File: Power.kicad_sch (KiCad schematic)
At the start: 24 parts, among them J10 Servo PW 7, J11 Servo PW 8, J3 1986660-2, J4 Servo PW 1, J5 Servo PW 2, J6 Servo PW 3, J7 Servo PW 4, J8 Servo PW 5, J9 Servo PW 6, U4 AP62301WU

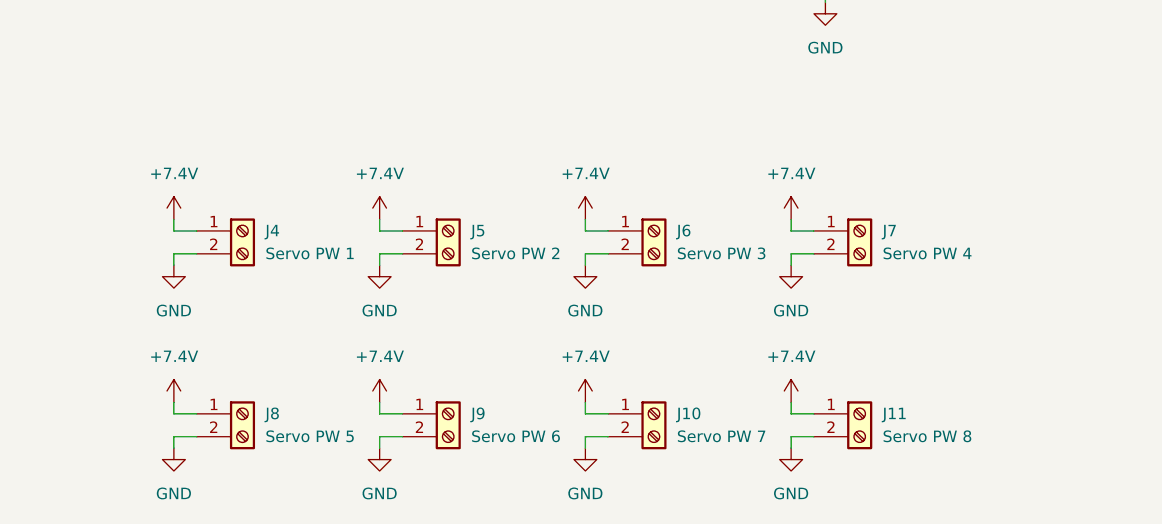
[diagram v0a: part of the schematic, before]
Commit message: Combine servo outputs to 3 pin terminal
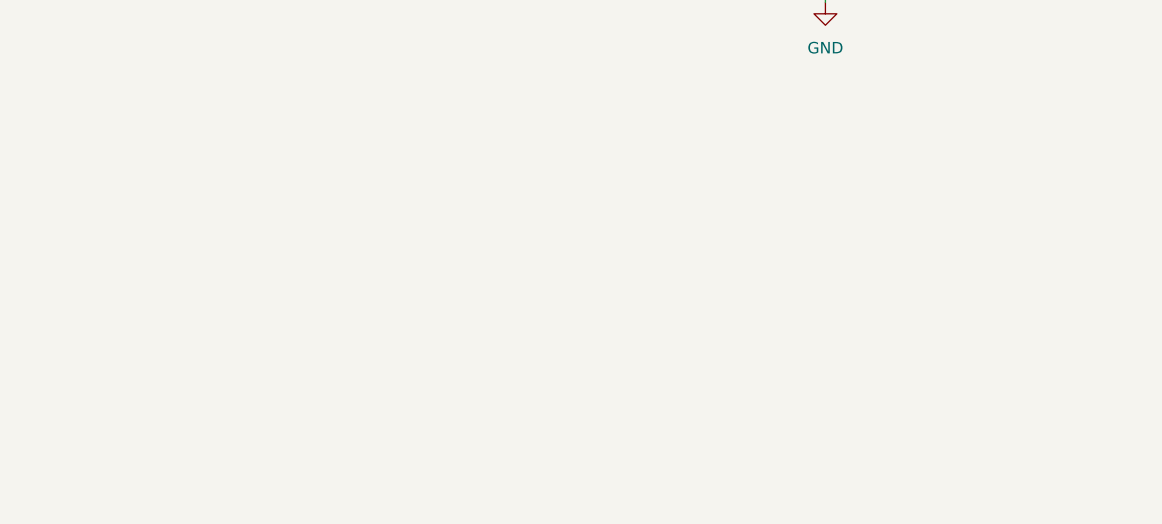
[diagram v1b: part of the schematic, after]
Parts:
- removed J10: Servo PW 7, TerminalBlock_Phoenix:TerminalBlock_Phoenix_MKDS-1,5-2_1x02_P5.00mm_Horizontal, symbol Connector:Screw_Terminal_01x02
- removed J11: Servo PW 8, TerminalBlock_Phoenix:TerminalBlock_Phoenix_MKDS-1,5-2_1x02_P5.00mm_Horizontal, symbol Connector:Screw_Terminal_01x02
- removed J4: Servo PW 1, TerminalBlock_Phoenix:TerminalBlock_Phoenix_MKDS-1,5-2_1x02_P5.00mm_Horizontal, symbol Connector:Screw_Terminal_01x02
- removed J5: Servo PW 2, TerminalBlock_Phoenix:TerminalBlock_Phoenix_MKDS-1,5-2_1x02_P5.00mm_Horizontal, symbol Connector:Screw_Terminal_01x02
- removed J6: Servo PW 3, TerminalBlock_Phoenix:TerminalBlock_Phoenix_MKDS-1,5-2_1x02_P5.00mm_Horizontal, symbol Connector:Screw_Terminal_01x02
- removed J7: Servo PW 4, TerminalBlock_Phoenix:TerminalBlock_Phoenix_MKDS-1,5-2_1x02_P5.00mm_Horizontal, symbol Connector:Screw_Terminal_01x02
- removed J8: Servo PW 5, TerminalBlock_Phoenix:TerminalBlock_Phoenix_MKDS-1,5-2_1x02_P5.00mm_Horizontal, symbol Connector:Screw_Terminal_01x02
- removed J9: Servo PW 6, TerminalBlock_Phoenix:TerminalBlock_Phoenix_MKDS-1,5-2_1x02_P5.00mm_Horizontal, symbol Connector:Screw_Terminal_01x02

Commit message: Add footprints to symbols
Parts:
- C18: footprint (none) -> Capacitor_SMD:C_1210_3225Metric; Listing (none) -> https://www.digikey.com/en/products/detail/samsung-electro-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
- C19, C21: footprint (none) -> Capacitor_SMD:C_1206_3216Metric; Listing (none) -> https://www.digikey.com/en/products/detail/samsung-electro-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
- C20, C24, C25: footprint (none) -> Capacitor_SMD:C_0603_1608Metric; Listing (none) -> https://www.digikey.com/en/products/detail/samsung-electro-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
- C22: footprint (none) -> Capacitor_SMD:C_0402_1005Metric; Listing (none) -> https://www.digikey.com/en/products/detail/samsung-electro-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
- C23: footprint (none) -> Capacitor_SMD:C_0402_1005Metric; Listing (none) -> https://www.digikey.com/en/products/detail/murata-electroni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
- CR1, U4: Listing (none) -> https://www.digikey.com/en/products/detail/diodes-incorpora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
- CR2: Listing (none) -> https://www.digikey.com/en/products/detail/vishay-general-s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
- D2: Listing (none) -> https://www.digikey.com/en/products/detail/microchip-techno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
- J3: Listing (none) -> https://www.digikey.com/en/products/detail/te-connectivity-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
- L1: footprint (none) -> Inductor_SMD:L_0805_2012Metric; Listing (none) -> https://www.digikey.com/en/products/detail/tdk-corporation/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
- R10: footprint (none) -> Resistor_SMD:R_0402_1005Metric; Listing (none) -> https://www.digikey.com/en/products/detail/stackpole-electr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
- R11: footprint (none) -> Resistor_SMD:R_0402_1005Metric; Listing (none) -> https://www.digikey.com/en/products/detail/yageo/RC0402FR-0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
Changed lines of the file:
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@@
 			)
 		)
-		(property "Footprint" ""
+		(property "Footprint" "Capacitor_SMD:C_0603_1608Metric"
 			(at 110.1852 48.26 0)
 			(effects
@@
 			)
 		)
-		(property "Datasheet" "~"
+		(property "Datasheet" "https://weblib.samsungsem.com/mlcc/mlcc-ec-data-sheet.do?partNumber=CL10B105KO8NNN"
 			(at 109.22 44.45 0)
 			(effects
@@
 		)
 		(property "Description" "Unpolarized capacitor"
+			(at 109.22 44.45 0)
+			(effects
+				(font
+					(size 1.27 1.27)
+				)
+				(hide yes)
+			)
+		)
+		(property "Listing" "https://www.digikey.com/en/products/detail/samsung-electro-mechanics/CL10B105KO8NNNC/3886677"
 			(at 109.22 44.45 0)
 			(effects
@@
 			)
 		)
-		(property "Footprint" ""
+		(property "Footprint" "Capacitor_SMD:C_0402_1005Metric"
 			(at 87.3252 102.87 0)
 			(effects
@@
 			)
 		)
-		(property "Datasheet" "~"
+		(property "Datasheet" "https://search.murata.co.jp/Ceramy/image/img/A01X/G101/ENG/GJM1555C1H100GB01-01.pdf"
 			(at 86.36 99.06 0)
 			(effects
@@
 		)
 		(property "Description" "Unpolarized capacitor"
+			(at 86.36 99.06 0)
+			(effects
+				(font
+					(size 1.27 1.27)
+				)
+				(hide yes)
+			)
+		)
+		(property "Listing" "https://www.digikey.com/en/products/detail/murata-electronics/GJM1555C1H100GB01D/2592846"
 			(at 86.36 99.06 0)
 			(effects
@@
 			)
 		)
+		(property "Listing" "https://www.digikey.com/en/products/detail/microchip-technology/APT60S20BG/1494822"
+			(at 67.31 40.64 0)
+			(effects
+				(font
+					(size 1.27 1.27)
+				)
+				(hide yes)
+			)
+		)
 		(pin "1"
 		)
@@
 			)
 		)
-		(property "Footprint" ""
+		(property "Footprint" "Capacitor_SMD:C_0603_1608Metric"
 			(at 115.2652 107.95 0)
 			(effects
@@
 			)
 		)
-		(property "Datasheet" "~"
+		(property "Datasheet" "https://mm.digikey.com/Volume0/opasdata/d220001/medias/docus/2901/CL10A226MP8NUNC_Spec.pdf"
 			(at 114.3 104.14 0)
 			(effects
@@
 		)
 		(property "Description" "Unpolarized capacitor"
+			(at 114.3 104.14 0)
+			(effects
+				(font
+					(size 1.27 1.27)
+				)
+				(hide yes)
+			)
+		)
+		(property "Listing" "https://www.digikey.com/en/products/detail/samsung-electro-mechanics/CL10A226MP8NUNE/3886932"
 			(at 114.3 104.14 0)
 			(effects
@@
 			)
 		)
-		(property "Footprint" ""
+		(property "Footprint" "Capacitor_SMD:C_1210_3225Metric"
 			(at 84.7852 48.26 0)
 			(effects
@@
 			)
 		)
-		(property "Datasheet" "~"
+		(property "Datasheet" "https://mm.digikey.com/Volume0/opasdata/d220001/medias/docus/42/CL32A107MPVNNNE_Spec.pdf"
 			(at 83.82 44.45 0)
 			(effects
@@
 		)
 		(property "Description" "Unpolarized capacitor"
+			(at 83.82 44.45 0)
+			(effects
+				(font
+					(size 1.27 1.27)
+				)
+				(hide yes)
+			)
+		)
+		(property "Listing" "https://www.digikey.com/en/products/detail/samsung-electro-mechanics/CL32A107MPVNNNE/3889022"
 			(at 83.82 44.45 0)
 			(effects
@@
 			)
 		)
-		(property "Footprint" ""
+		(property "Footprint" "Capacitor_SMD:C_1206_3216Metric"
 			(at 37.1348 102.87 0)
 			(effects
@@
 			)
 		)
-		(property "Datasheet" "~"
+		(property "Datasheet" "https://mm.digikey.com/Volume0/opasdata/d220001/medias/docus/658/CL31B106KAHNNNE_Spec.pdf"
 			(at 38.1 99.06 0)
 			(effects
@@
 		)
 		(property "Description" "Unpolarized capacitor"
+			(at 38.1 99.06 0)
+			(effects
+				(font
+					(size 1.27 1.27)
+				)
+				(hide yes)
+			)
+		)
+		(property "Listing" "https://www.digikey.com/en/products/detail/samsung-electro-mechanics/CL31B106KAHNNNE/3887462"
 			(at 38.1 99.06 0)
 			(effects
@@
 			)
 		)
-		(property "Footprint" ""
+		(property "Footprint" "Inductor_SMD:L_0805_2012Metric"
 			(at 80.01 93.98 0)
 			(effects
@@
 			)
 		)
-		(property "Datasheet" "~"
+		(property "Datasheet" "https://product.tdk.com/en/system/files/dam/doc/product/inductor/inductor/smd/catalog/inductor_automotive_decoupling_mlz2012-a_en.pdf"
 			(at 80.01 93.98 0)
 			(effects
@@
 		(property "Description" "Inductor"
 			(at 80.01 93.98 0)
+			(effects
+				(font
+					(size 1.27 1.27)
+				)
+				(hide yes)
+			)
+		)
+		(property "Listing" "https://www.digikey.com/en/products/detail/tdk-corporation/MLZ2012M3R3ATD69/9605952"
+			(at 80.01 93.98 90)
 			(effects
 				(font
@@
 			)
 		)
-		(property "Footprint" ""
+		(property "Footprint" "Resistor_SMD:R_0402_1005Metric"
 			(at 103.886 109.474 90)
 			(effects
@@
 			)
 		)
-		(property "Datasheet" "~"
+		(property "Datasheet" "https://www.yageogroup.com/content/datasheet/asset/file/PYU-RC_GROUP_51_ROHS_L"
 			(at 102.87 109.22 0)
 			(effects
@@
 		)
 		(property "Description" "Resistor, US symbol"
+			(at 102.87 109.22 0)
+			(effects
+				(font
+					(size 1.27 1.27)
+				)
+				(hide yes)
+			)
+		)
+		(property "Listing" "https://www.digikey.com/en/products/detail/yageo/RC0402FR-0710KL/726523"
 			(at 102.87 109.22 0)
 			(effects
@@
 			)
 		)
+		(property "Listing" "https://www.digikey.com/en/products/detail/diodes-incorporated/AP62301WU-7/12349279?s=N4IgTCBcDaIIIAUBsYDMAGAjAdQKogF0BfIA"
+			(at 55.88 96.52 0)
+			(effects
+				(font
+					(size 1.27 1.27)
+				)
+				(hide yes)
+			)
+		)
 		(pin "3"
 		)
@@
 			)
 		)
-		(property "Footprint" ""
+		(property "Footprint" "Capacitor_SMD:C_0603_1608Metric"
 			(at 127.9652 107.95 0)
 			(effects
@@
 			)
 		)
-		(property "Datasheet" "~"
+		(property "Datasheet" "https://mm.digikey.com/Volume0/opasdata/d220001/medias/docus/2901/CL10A226MP8NUNC_Spec.pdf"
 			(at 127 104.14 0)
 			(effects
@@
 		)
 		(property "Description" "Unpolarized capacitor"
+			(at 127 104.14 0)
+			(effects
+				(font
+					(size 1.27 1.27)
+				)
+				(hide yes)
+			)
+		)
+		(property "Listing" "https://www.digikey.com/en/products/detail/samsung-electro-mechanics/CL10A226MP8NUNE/3886932"
 			(at 127 104.14 0)
 			(effects
@@
 			)
 		)
-		(property "Footprint" ""
+		(property "Footprint" "Resistor_SMD:R_0402_1005Metric"
 			(at 103.886 99.314 90)
 			(effects
@@
 			)
 		)
-		(property "Datasheet" "~"
+		(property "Datasheet" "https://www.seielect.com/catalog/SEI-RMCF_RMCP.pdf"
 			(at 102.87 99.06 0)
 			(effects
@@
 		)
 		(property "Description" "Resistor, US symbol"
+			(at 102.87 99.06 0)
+			(effects
+				(font
+					(size 1.27 1.27)
+				)
+				(hide yes)
+			)
+		)
+		(property "Listing" "https://www.digikey.com/en/products/detail/stackpole-electronics-inc/RMCF0402FT31K6/1714647"
 			(at 102.87 99.06 0)
 			(effects
@@
 			)
 		)
+		(property "Listing" "https://www.digikey.com/en/products/detail/vishay-general-semiconductor-diodes-division/MSP3V3-M3-89A/2071748"
+			(at 143.51 104.14 90)
+			(effects
+				(font
+					(size 1.27 1.27)
+				)
+				(hide yes)
+			)
+		)
 		(pin "2"
 		)
@@
 			)
 		)
-		(property "Footprint" ""
+		(property "Footprint" "Capacitor_SMD:C_0402_1005Metric"
 			(at 74.93 87.9348 0)
 			(effects
@@
 			)
 		)
-		(property "Datasheet" "~"
+		(property "Datasheet" "https://mm.digikey.com/Volume0/opasdata/d220001/medias/docus/503/CL05A104KA5NNNC.pdf"
 			(at 71.12 88.9 0)
 			(effects
@@
 		(property "Description" "Unpolarized capacitor"
 			(at 71.12 88.9 0)
+			(effects
+				(font
+					(size 1.27 1.27)
+				)
+				(hide yes)
+			)
+		)
+		(property "Listing" "https://www.digikey.com/en/products/detail/samsung-electro-mechanics/CL05A104KA5NNNC/3886701"
+			(at 71.12 88.9 90)
 			(effects
 				(font
@@
 			)
 		)
-		(property "Footprint" ""
+		(property "Footprint" "Capacitor_SMD:C_1206_3216Metric"
 			(at 97.4852 48.26 0)
 			(effects
@@
 			)
 		)
-		(property "Datasheet" "~"
+		(property "Datasheet" "https://mm.digikey.com/Volume0/opasdata/d220001/medias/docus/658/CL31B106KAHNNNE_Spec.pdf"
 			(at 96.52 44.45 0)
 			(effects
@@
 		)
 		(property "Description" "Unpolarized capacitor"
+			(at 96.52 44.45 0)
+			(effects
+				(font
+					(size 1.27 1.27)
+				)
+				(hide yes)
+			)
+		)
+		(property "Listing" "https://www.digikey.com/en/products/detail/samsung-electro-mechanics/CL31B106KAHNNNE/3887462"
 			(at 96.52 44.45 0)
 			(effects
@@
 			)
 		)
+		(property "Listing" "https://www.digikey.com/en/products/detail/te-connectivity-amp-connectors/1986660-2/4021603"
+			(at 44.45 44.45 0)
+			(effects
+				(font
+					(size 1.27 1.27)
+				)
+				(hide yes)
+			)
+		)
 		(pin "2B"
 		)
@@
 			(effects
 				(font
+					(size 1.27 1.27)
+				)
+				(hide yes)
+			)
+		)
+		(property "Listing" "https://www.digikey.com/en/products/detail/diodes-incorporated/SMBJ7-5A-13-F/749992"
+			(at 76.2 53.34 90)
+			(effects
+				(font

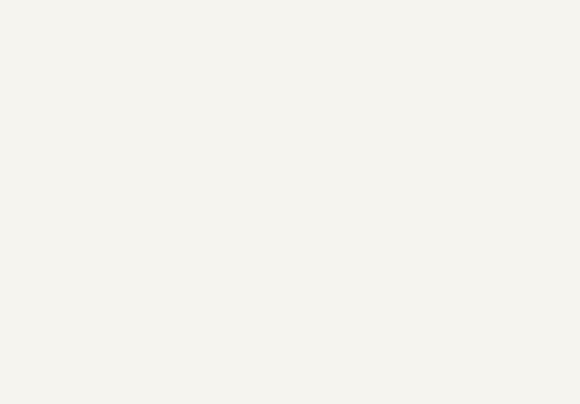
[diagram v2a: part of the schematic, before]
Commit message: Add test points
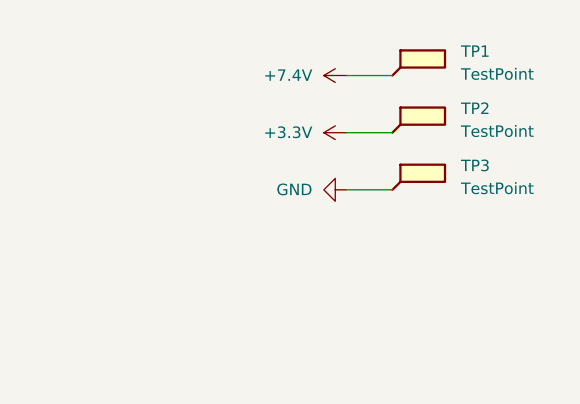
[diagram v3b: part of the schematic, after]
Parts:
- added TP1, TP2, TP3: TestPoint, TestPoint:TestPoint_Plated_Hole_D2.0mm, symbol Connector:TestPoint_Flag
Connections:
- net +3.3V: now also TP2.1
- net +7.4V: now also TP1.1
- net GND: now also TP3.1

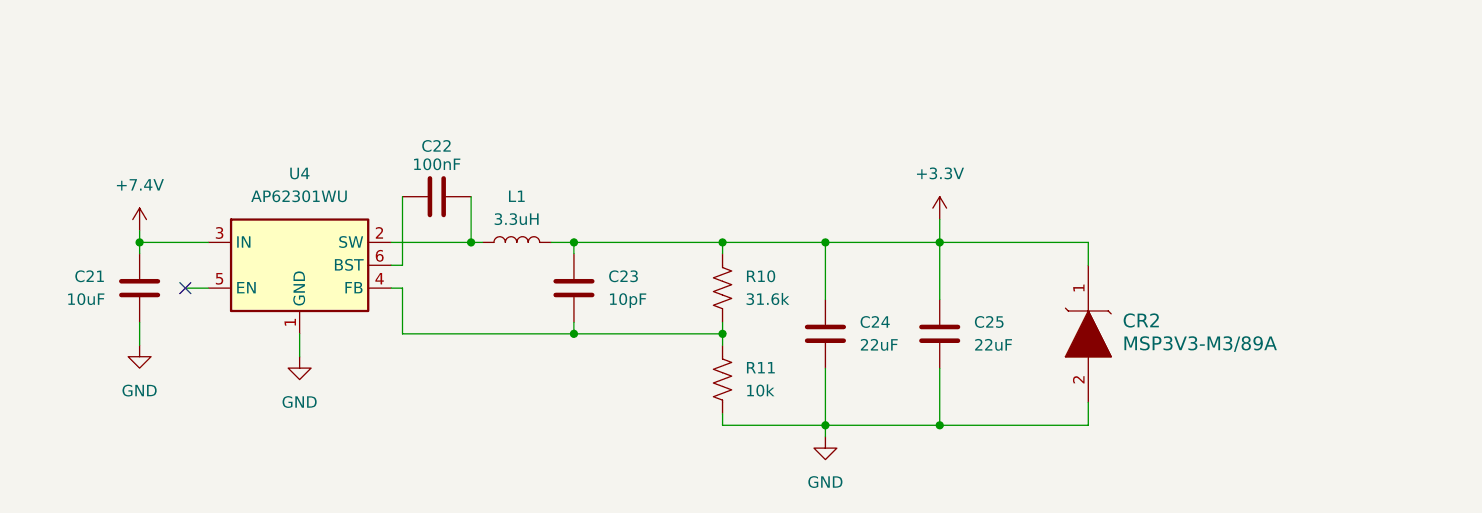
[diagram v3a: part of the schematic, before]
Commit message: Switch from variable to fixed 3.3V buck converter
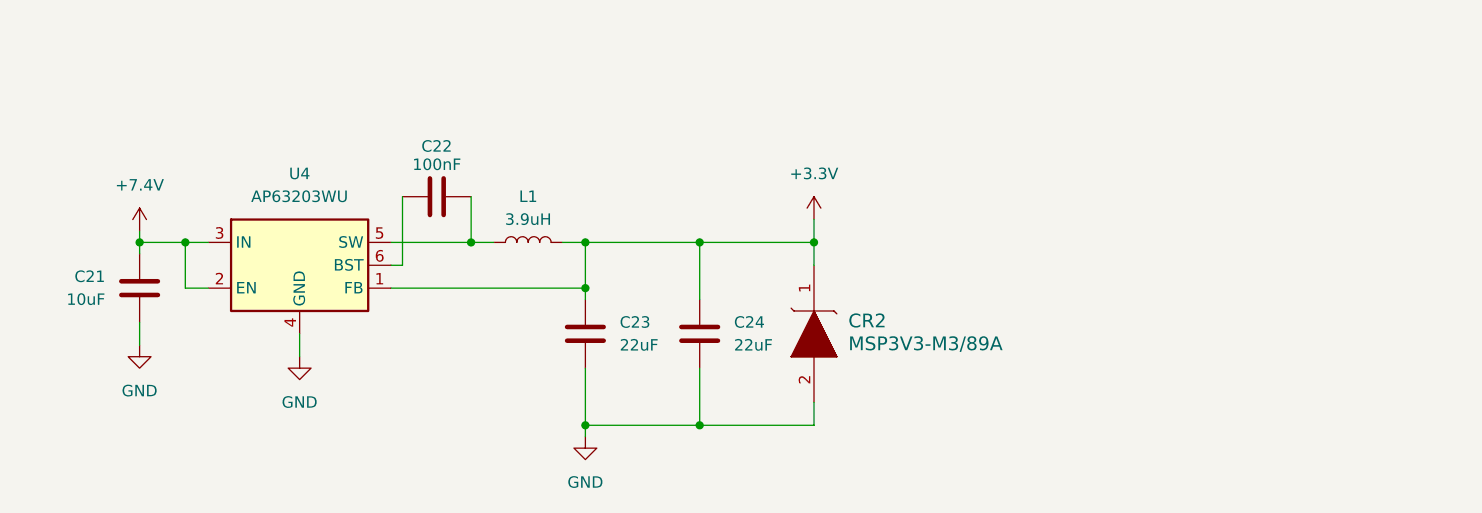
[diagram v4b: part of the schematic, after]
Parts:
- removed C23: 10pF, Capacitor_SMD:C_0402_1005Metric, symbol Device:C
- removed R10: 31.6k, Resistor_SMD:R_0402_1005Metric, symbol Device:R_US
- removed R11: 10k, Resistor_SMD:R_0402_1005Metric, symbol Device:R_US
- removed U4: AP62301WU, Package_TO_SOT_SMD:TSOT-23-6, symbol Regulator_Switching:AP62301WU
- added U4: AP63203WU, Package_TO_SOT_SMD:TSOT-23-6, symbol Regulator_Switching:AP63203WU
- L1: value 3.3uH -> 3.9uH; footprint Inductor_SMD:L_0805_2012Metric -> Inductor_SMD:L_Pulse_PA4334; Listing https://www.digikey.com/en/products/detail/tdk-corporation/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 -> https://www.digikey.com/en/products/detail/pulse-electronic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
- renumbered C24 to C23, C25 to C24
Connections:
- net +3.3V: now also U4.1 (FB)
- net +7.4V: now also U4.2 (EN), U4.3 (IN)
- net GND: now also U4.4 (GND)
- net at C22.2, L1.1: now also U4.5 (SW)
- net at C22.1: now also U4.6 (BST)
- no-connect marks 1 -> 0
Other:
- moved on the sheet: C23, C24, CR2, L1
